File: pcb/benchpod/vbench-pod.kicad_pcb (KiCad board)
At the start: 4 copper layers, 100 x 80 mm, 505 parts, among them J1 Conn_02x10_Odd_Even, J4 Screw_Terminal_01x02, J5 Screw_Terminal_01x02, J6 Screw_Terminal_01x02, J7 HR911105A_C12074, J8 Screw_Terminal_01x02, J9 Screw_Terminal_01x02, K1 G6K-2F-Y DC5, K2 G6K-2F-Y DC5, K3 G6K-2F-Y DC5, K4 G6K-2F-Y DC5, Q1 BCP56, SW1 TS-1088-AR02016, SW2 TS-1088-AR02016, U1 ICE40UP5K-SG48ITR, U10 TCAN1044VDRBRQ1, U18 SN74LVC2G66DCUR, U19 SN74LVC2G66DCUR, U2 W25Q64JVSSIQ, U20 SN74LVC2G66DCUR, U21 SN74LVC2G66DCUR, U22 SRV05-4.TCT, U23 SRV05-4.TCT, U24 SN74LVC2G66DCUR, U25 SRV05-4.TCT, U26 TPS259470ARPWR, U27 TPS259470ARPWR, U29 INA238AIDGSR, U3 TPS7A2050PDBVR, U30 TPS82130SILR, U31 AP2112K-1.2, U32 AP2112K-2.5TRG1, U33 INA238AIDGSR, U34 SRV05-4.TCT, U36 MCP33131D-10-E/MS, U37 THS4551IDGKR, U38 ADR4540BRZ-R7, U39 AP2112K-1.8TRG1, U4 ESP32-C3-MINI-1-N4, U40 OPA810IDBVR, U41 LM27761DSGR, U42 LM7705MM/NOPB, U43 DAC8551IADGKR, U44 OPA2365AIDR, U45 OPA2992IDR, U46 AP2112K-3.3, U47 TMUX1104DGSR, U48 TMUX1104DGSR, U49 TPS65131TRGERQ1, U5 STM32H563ZIT6, U50 TPS7A1901DRBR, U51 OPA2992IDR, U52 AP2112K-1.8TRG1, U53 TPL7407LAPWR, U54 TCA9554PWR, U55 TCA9554PWR, U56 TCA9554PWR, U57 TPS259470ARPWR, U58 TCA9554PWR, U6 LAN8742AI-CZ-TR, U7 APS6404L-3SQR-SN_C5333729, U8 TPS2116DRLR, U9 XTR116UA/2K5, X1 SX3M48.000B10F20TNN, Y1 Crystal_GND24, Y2 Crystal_GND24

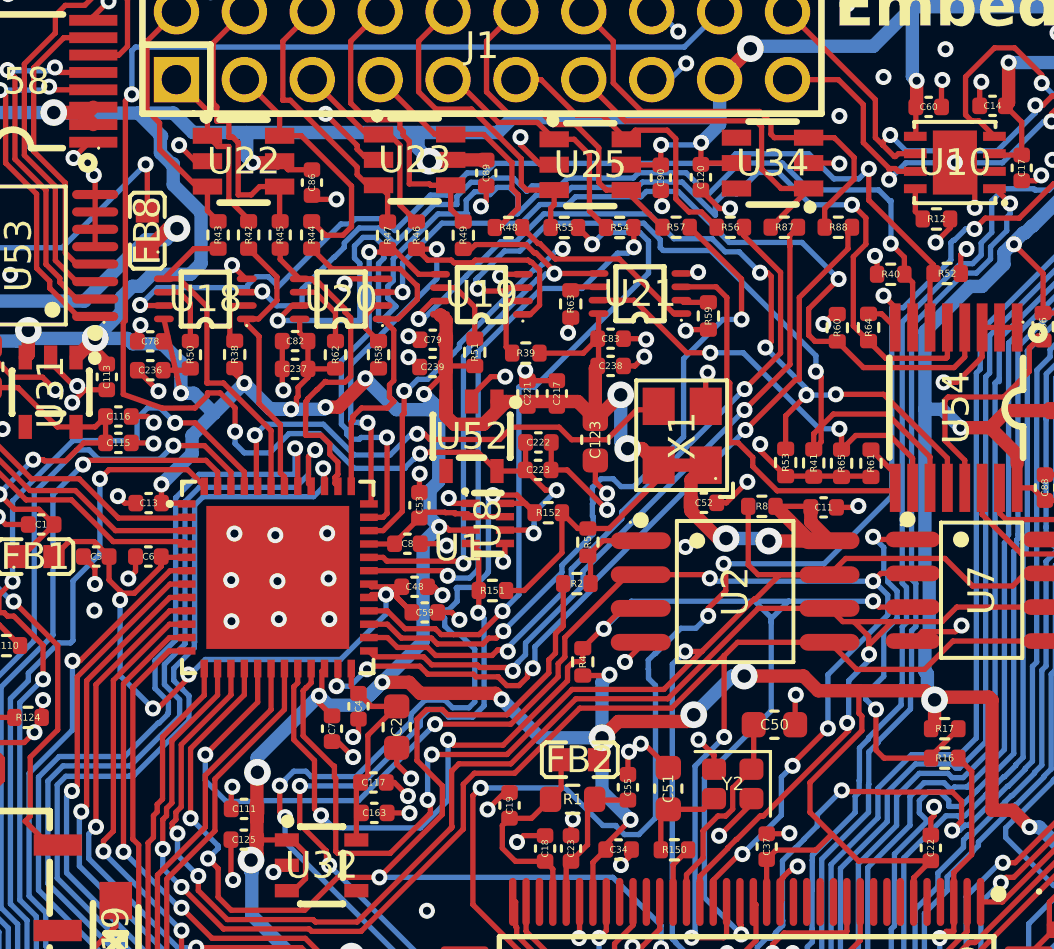
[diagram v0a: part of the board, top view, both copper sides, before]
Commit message: 1V8/3V3 pull-ups / pull-down fixes
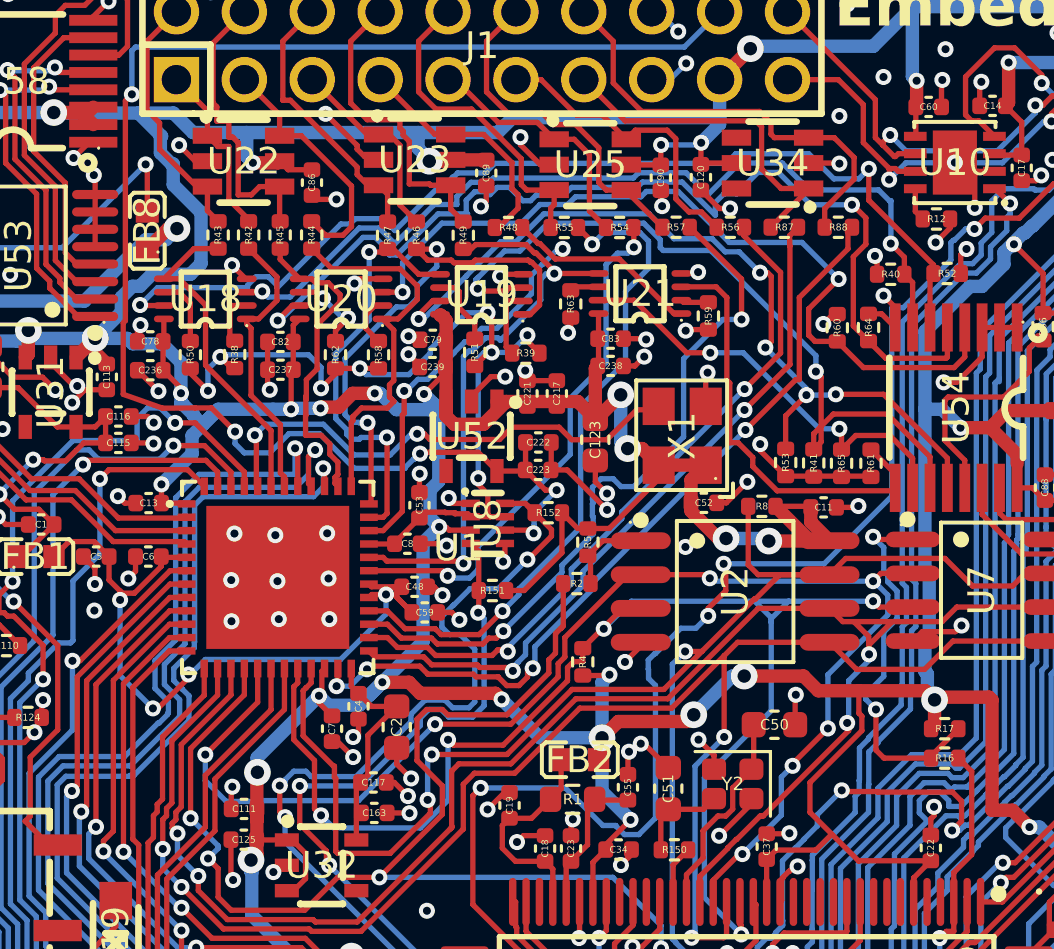
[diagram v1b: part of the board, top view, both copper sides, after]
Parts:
- moved C237 0.55 mm to (78.7, 34.9)
- moved C82 0.55 mm to (78.7, 33.9)
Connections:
- C53 pad 2: /LA_VCCIO -> LA_VCCIO
- C8 pad 2: /LA_VCCIO -> LA_VCCIO
- R38 pad 1: +3V3 -> LA_VCCIO
- R39 pad 1: +3V3 -> LA_VCCIO
- R50 pad 2: +3V3 -> LA_VCCIO
- R51 pad 2: +3V3 -> LA_VCCIO
- R58 pad 1: +3V3 -> LA_VCCIO
- R62 pad 2: +3V3 -> LA_VCCIO
- U1 pad 33: /LA_VCCIO -> LA_VCCIO
- U8 pad 2: /LA_VCCIO -> LA_VCCIO
- U8 pad 7: /LA_VCCIO -> LA_VCCIO
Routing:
- net LA_VCCIO: track 0.00 -> 33.8 mm, vias 0 -> 8
- net +3V3: track 898.8 -> 889.5 mm, vias 90 -> 89
- net /LogicAnalyzer/CTRL3: track 46.5 -> 38.2 mm
- net /LA_VCCIO: track 5.65 -> 0.00 mm
- net /LogicAnalyzer/CTRL2: track 34.7 -> 33.5 mm
- net +1V8: track 59.7 -> 58.6 mm
- net /LA_OUT9: track 20.6 -> 19.7 mm
- net /LA_VCCIO_ST: track 61.5 -> 60.7 mm
- net Net-(U20-2B): track 2.72 -> 3.27 mm, vias 0 -> 2

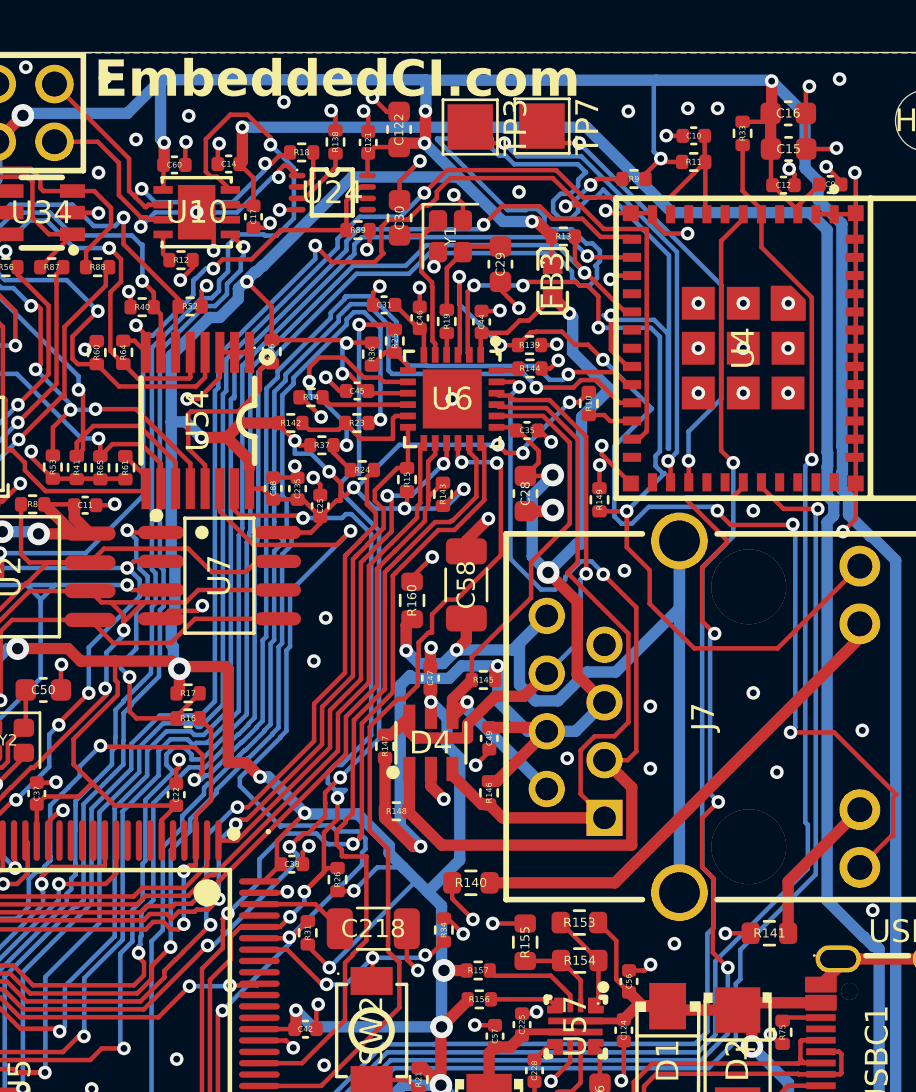
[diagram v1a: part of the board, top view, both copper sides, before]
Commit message: ethernet rx/tx reroute
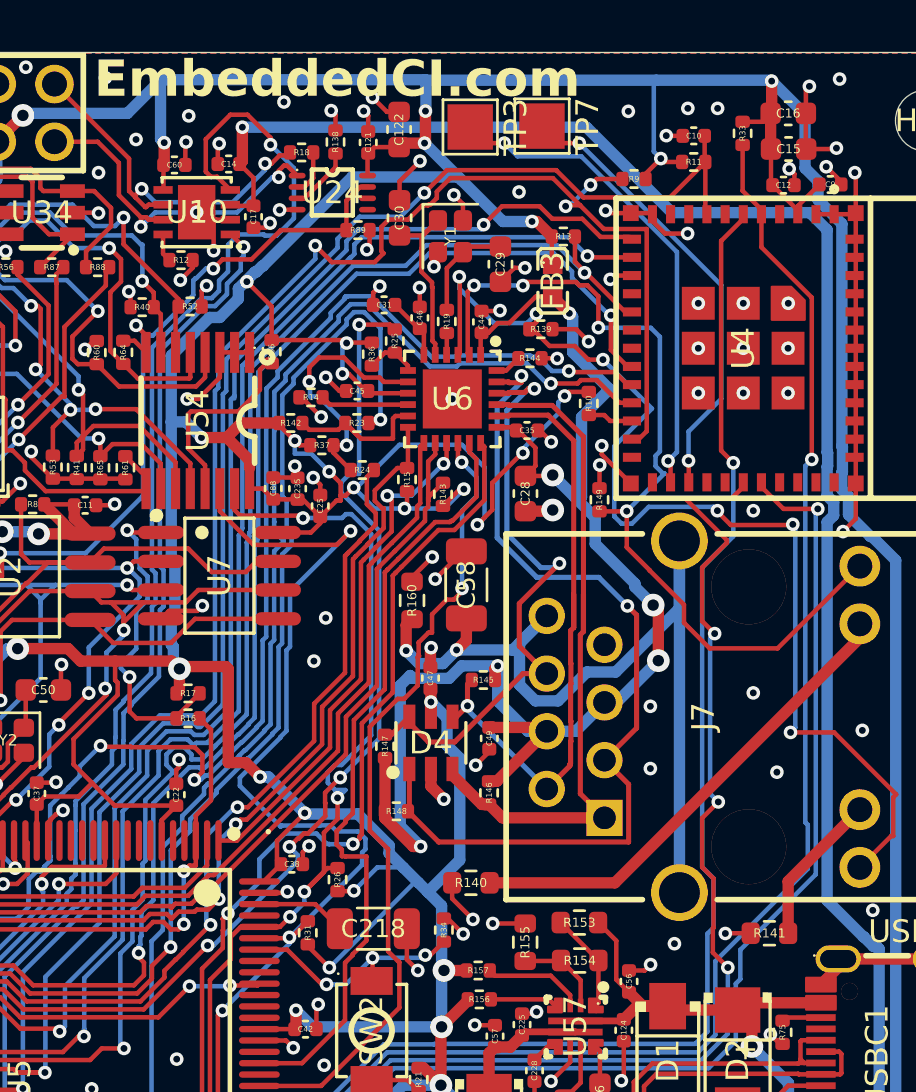
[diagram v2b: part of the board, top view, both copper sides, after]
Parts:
- moved R139 0.86 mm to (119.1, 32.3)
- moved R144 0.45 mm to (118.6, 33.6)
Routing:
- net /ESP32_CTS: track 120.4 -> 76.2 mm
- net +3V3: track 889.5 -> 895.0 mm
- net /Ethernet/TXN: track 24.1 -> 28.4 mm
- net /Ethernet/VDDA: track 66.1 -> 63.9 mm, vias 5 -> 6
- net /RMII_TX_EN: track 37.6 -> 35.7 mm
- net /Ethernet/RXN: track 25.7 -> 27.2 mm, vias 1 -> 2
- net /ESP32_MOSI: track 76.6 -> 75.4 mm
- net /Ethernet/RXP: track 40.9 -> 39.7 mm
- net GND: track 515.7 -> 516.9 mm, vias 496 -> 494
- net /ESP32_SCLK: track 75.3 -> 74.3 mm
- net /Ethernet/TXP: track 31.5 -> 30.8 mm
